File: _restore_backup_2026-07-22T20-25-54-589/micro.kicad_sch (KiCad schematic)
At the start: 17 parts, among them J7 USB_C_Receptacle_USB2.0_16P, J8 Conn_01x04_Pin, J9 Conn_01x06_Pin, U4 STM32G473CETx

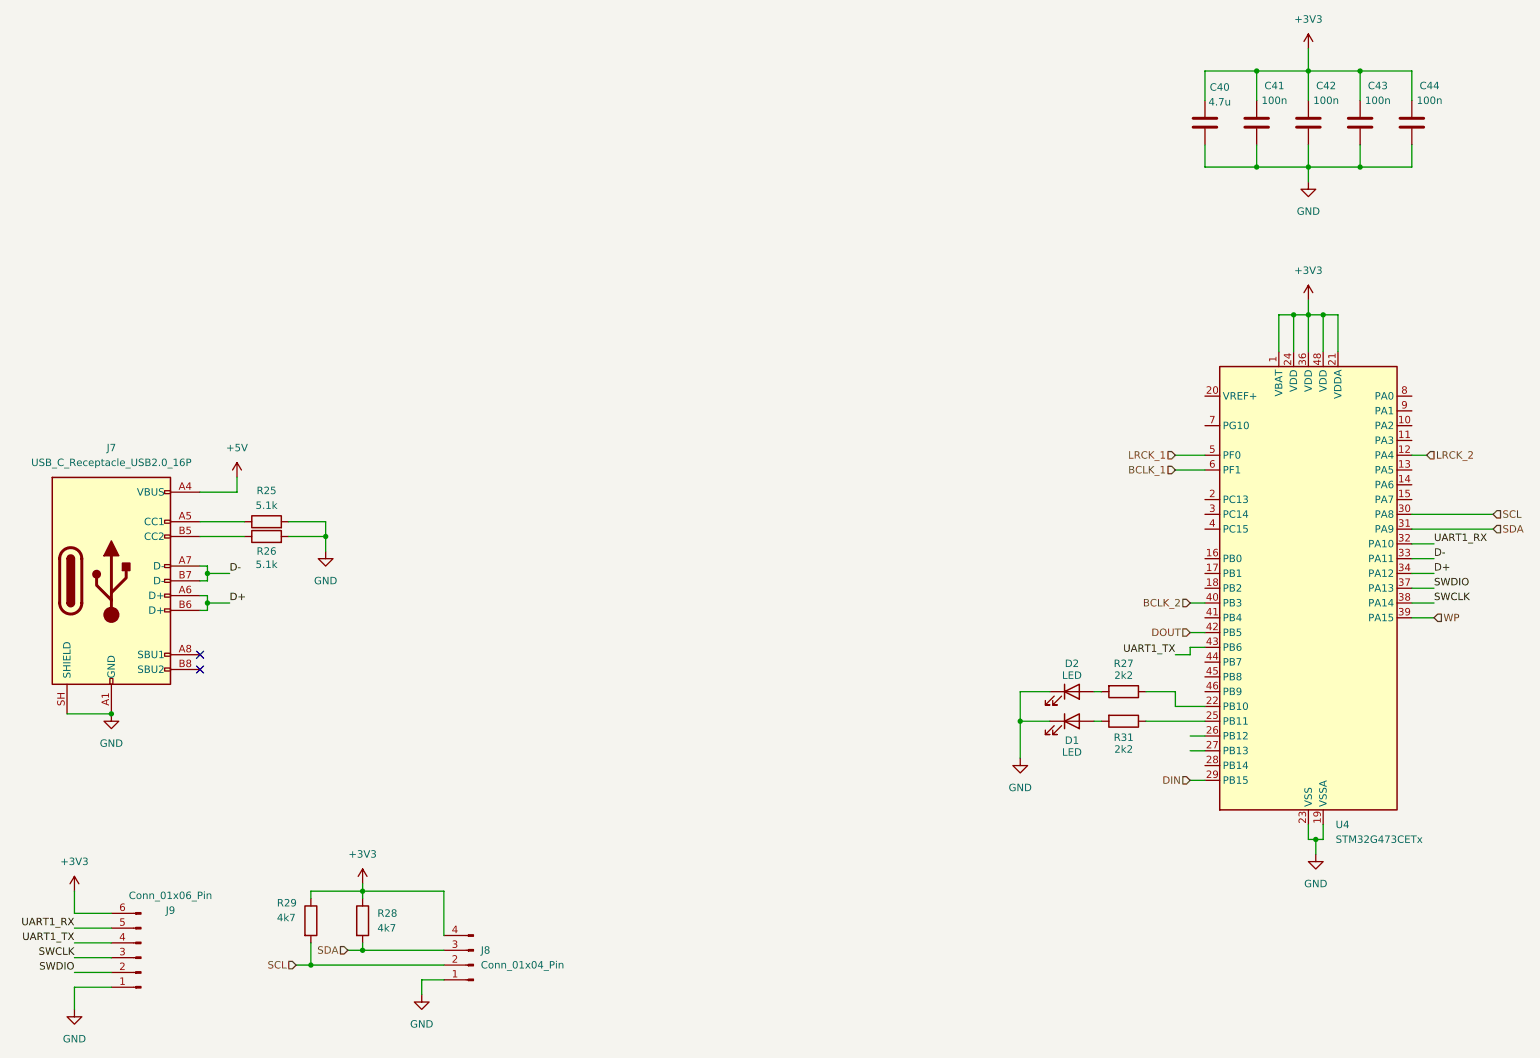
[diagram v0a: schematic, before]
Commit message: aggiunto cad 3d dei connettori
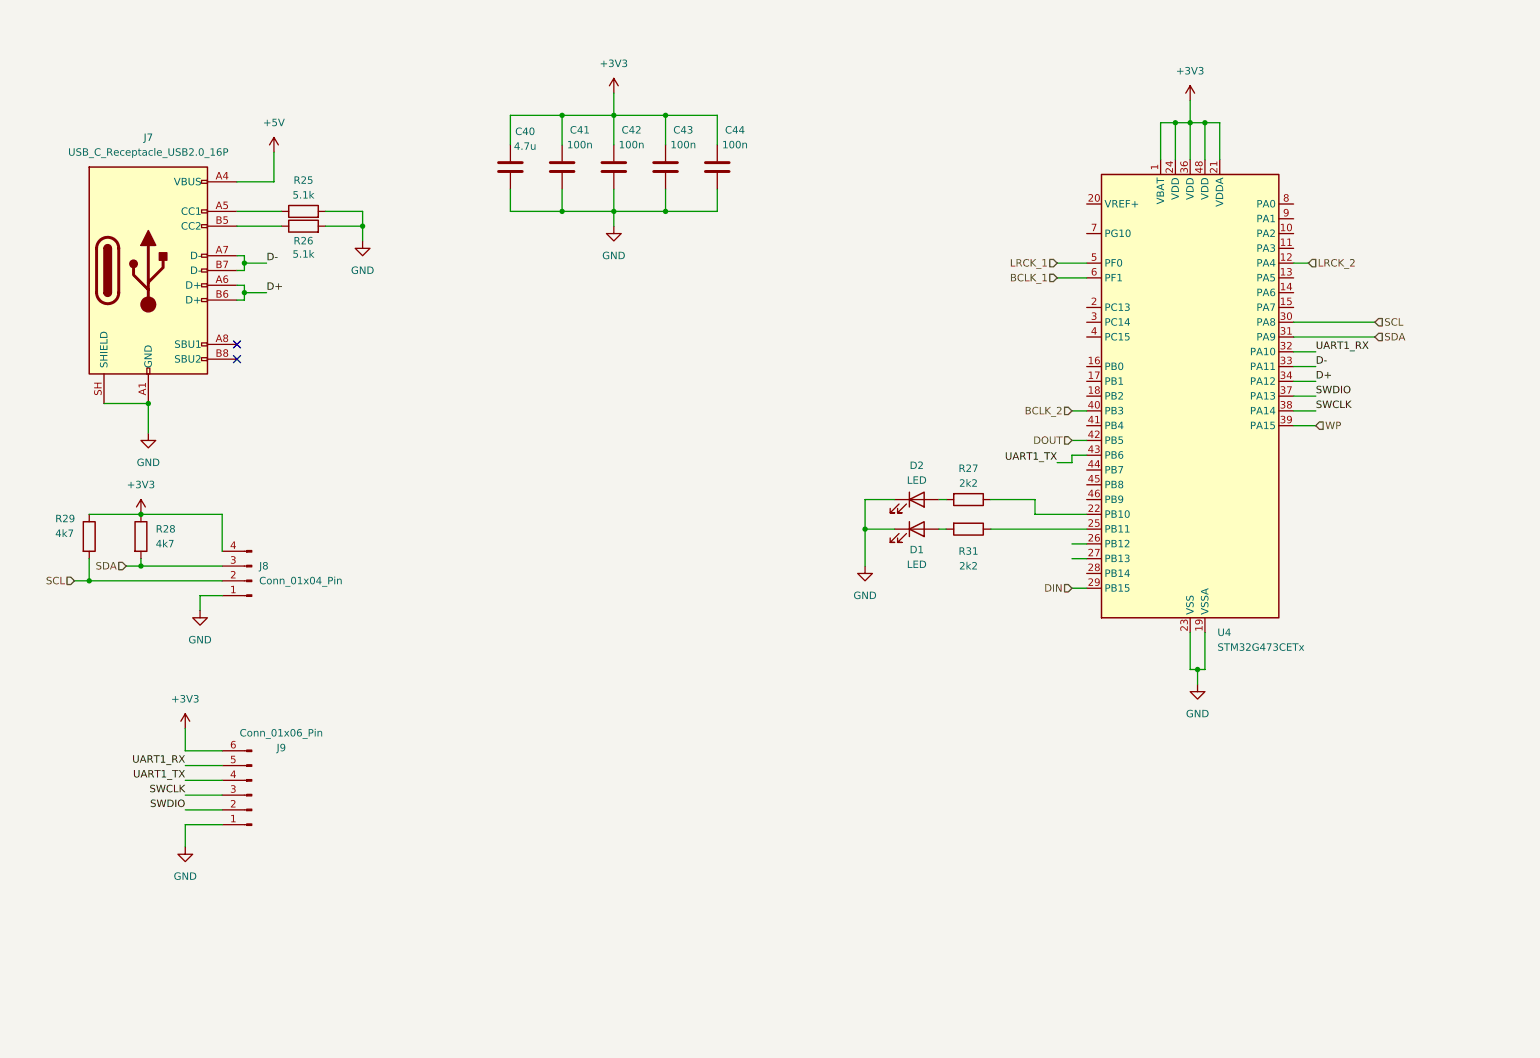
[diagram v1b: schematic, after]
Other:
- moved on the sheet: C40, C41, C42, C43, C44, D1, D2, J7, J8, J9, R25, R26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
